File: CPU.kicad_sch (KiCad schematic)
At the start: 12 parts, among them U3 MOS6502

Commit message: update traces
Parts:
- B11, C11, C14: footprint Apple:DIP-14_W7.62mm -> Package_DIP:DIP-14_W7.62mm
- B6, B7, H10, H11, H3, H4, H5: footprint Apple:DIP-16_W7.62mm -> Package_DIP:DIP-16_W7.62mm
- H7: renamed from U3; footprint Apple:DIP-40_W15.24mm -> Package_DIP:DIP-40_W15.24mm
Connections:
- net ~{RDY} renamed RDY
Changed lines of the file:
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@@
   (junction (at 177.292 107.95) (diameter 0) (color 0 0 0 0)
   )
+  (junction (at 213.36 114.3) (diameter 0) (color 0 0 0 0)
+  )
   (junction (at 134.112 94.234) (diameter 0) (color 0 0 0 0)
   )
@@
   (junction (at 270.256 110.49) (diameter 0) (color 0 0 0 0)
   )
+  (junction (at 222.25 129.54) (diameter 0) (color 0 0 0 0)
+  )
   (junction (at 270.51 82.55) (diameter 0) (color 0 0 0 0)
   )
@@
   (junction (at 270.256 137.668) (diameter 0) (color 0 0 0 0)
   )
+  (junction (at 215.9 123.444) (diameter 0) (color 0 0 0 0)
+  )
   (bus_entry (at 138.43 252.73) (size 2.54 2.54)
     (stroke (width 0) (type default))
@@
     (stroke (width 0) (type default))
   )
+  (wire (pts (xy 215.9 123.444) (xy 215.9 116.84))
+    (stroke (width 0) (type default))
+  )
   (wire (pts (xy 165.608 126.238) (xy 156.972 126.238))
     (stroke (width 0) (type default))
@@
     (stroke (width 0) (type default))
   )
+  (wire (pts (xy 215.392 123.444) (xy 215.9 123.444))
+    (stroke (width 0) (type default))
+  )
   (wire (pts (xy 268.224 159.004) (xy 271.78 159.004))
     (stroke (width 0) (type default))
@@
     (stroke (width 0) (type default))
   )
-  (wire (pts (xy 215.9 127) (xy 215.9 116.84))
+  (wire (pts (xy 215.9 127) (xy 215.9 123.444))
     (stroke (width 0) (type default))
   )
@@
     (stroke (width 0) (type default))
   )
+  (wire (pts (xy 222.25 129.54) (xy 222.25 130.302))
+    (stroke (width 0) (type default))
+  )
   (wire (pts (xy 165.608 121.158) (xy 156.972 121.158))
     (stroke (width 0) (type default))
@@
     (stroke (width 0) (type default))
   )
-  (wire (pts (xy 222.25 129.54) (xy 222.25 121.92))
+  (wire (pts (xy 222.25 121.92) (xy 222.25 129.54))
     (stroke (width 0) (type default))
   )
@@
   )
   (wire (pts (xy 248.92 97.79) (xy 256.032 97.79))
+    (stroke (width 0) (type default))
+  )
+  (wire (pts (xy 213.106 114.3) (xy 213.36 114.3))
     (stroke (width 0) (type default))
   )
@@
     (effects (font (size 1.27 1.27)) (justify left))
     (property "Intersheetrefs" "${INTERSHEET_REFS}" (at 200.66 124.46 0)
+      (effects (font (size 1.27 1.27)) hide)
+    )
+  )
+  (global_label "~{IRQ}" (shape output) (at 215.392 123.444 180)
+    (effects (font (size 0.9906 0.9906)) (justify right))
+    (property "Intersheetrefs" "${INTERSHEET_REFS}" (at 215.392 123.444 0)
       (effects (font (size 1.27 1.27)) hide)
     )
@@
     )
   )
+  (global_label "RDY" (shape output) (at 222.25 130.302 270)
+    (effects (font (size 0.9906 0.9906)) (justify right))
+    (property "Intersheetrefs" "${INTERSHEET_REFS}" (at 222.25 130.302 0)
+      (effects (font (size 1.27 1.27)) hide)
+    )
+  )
   (global_label "~{KBD}" (shape input) (at 44.704 260.35 180)
     (effects (font (size 1.27 1.27)) (justify right))
@@
     (effects (font (size 1.27 1.27)) (justify left))
     (property "Intersheetrefs" "${INTERSHEET_REFS}" (at 304.546 83.566 0)
+      (effects (font (size 1.27 1.27)) hide)
+    )
+  )
+  (global_label "~{NMI}" (shape output) (at 213.106 114.3 180)
+    (effects (font (size 0.9906 0.9906)) (justify right))
+    (property "Intersheetrefs" "${INTERSHEET_REFS}" (at 213.106 114.3 0)
       (effects (font (size 1.27 1.27)) hide)
     )
@@
       (effects (font (size 1.27 1.27)))
     )
-    (property "Footprint" "Apple:DIP-14_W7.62mm" (at 201.422 98.044 0)
+    (property "Footprint" "Package_DIP:DIP-14_W7.62mm" (at 201.422 98.044 0)
       (effects (font (size 1.27 1.27)) hide)
     )
@@
       (effects (font (size 1.27 1.27)))
     )
-    (property "Footprint" "Apple:DIP-14_W7.62mm" (at 189.484 107.95 0)
+    (property "Footprint" "Package_DIP:DIP-14_W7.62mm" (at 189.484 107.95 0)
       (effects (font (size 1.27 1.27)) hide)
     )
@@
       (effects (font (size 1.27 1.27)))
     )
-    (property "Footprint" "Apple:DIP-16_W7.62mm" (at 282.194 89.662 0)
+    (property "Footprint" "Package_DIP:DIP-16_W7.62mm" (at 282.194 89.662 0)
       (effects (font (size 1.27 1.27)) hide)
     )
@@
       (effects (font (size 1.27 1.27)))
     )
-    (property "Footprint" "Apple:DIP-16_W7.62mm" (at 146.812 86.614 0)
+    (property "Footprint" "Package_DIP:DIP-16_W7.62mm" (at 146.812 86.614 0)
       (effects (font (size 1.27 1.27)) hide)
     )
@@
       (effects (font (size 1.27 1.27)))
     )
-    (property "Footprint" "Apple:DIP-16_W7.62mm" (at 146.812 127.254 0)
+    (property "Footprint" "Package_DIP:DIP-16_W7.62mm" (at 146.812 127.254 0)
       (effects (font (size 1.27 1.27)) hide)
     )
@@
       (effects (font (size 1.27 1.27)))
     )
-    (property "Footprint" "Apple:DIP-16_W7.62mm" (at 282.194 117.602 0)
+    (property "Footprint" "Package_DIP:DIP-16_W7.62mm" (at 282.194 117.602 0)
       (effects (font (size 1.27 1.27)) hide)
     )
@@
       (effects (font (size 1.27 1.27)))
     )
-    (property "Footprint" "Apple:DIP-16_W7.62mm" (at 282.702 144.78 0)
+    (property "Footprint" "Package_DIP:DIP-16_W7.62mm" (at 282.702 144.78 0)
       (effects (font (size 1.27 1.27)) hide)
     )
@@
       (effects (font (size 1.27 1.27)))
     )
-    (property "Footprint" "Apple:DIP-14_W7.62mm" (at 260.35 63.5 0)
+    (property "Footprint" "Package_DIP:DIP-14_W7.62mm" (at 260.35 63.5 0)
       (effects (font (size 1.27 1.27)) hide)
     )
@@
       (effects (font (size 1.27 1.27)))
     )
-    (property "Footprint" "Apple:DIP-16_W7.62mm" (at 67.31 245.11 0)
+    (property "Footprint" "Package_DIP:DIP-16_W7.62mm" (at 67.31 245.11 0)
       (effects (font (size 1.27 1.27)) hide)
     )
@@
   (symbol (lib_id "AppleII-rescue:MOS6502-AppleII") (at 236.22 110.49 0) (unit 1)
     (in_bom yes) (on_board yes) (dnp no)
-    (property "Reference" "U3" (at 245.11 74.676 0)
+    (property "Reference" "H7" (at 245.11 74.676 0)
       (effects (font (size 1.27 1.27)))
     )
@@
       (effects (font (size 1.27 1.27)))
     )
-    (property "Footprint" "Apple:DIP-40_W15.24mm" (at 236.22 148.59 0)
+    (property "Footprint" "Package_DIP:DIP-40_W15.24mm" (at 236.22 148.59 0)
       (effects (font (size 1.27 1.27)) hide)
     )
@@
       (project "AppleII"
         (path "/f1f08369-4db3-46f7-9b89-a5d3cfbed55a/00000000-0000-0000-0000-00005fe9ff4d"
-          (reference "U3") (unit 1)
+          (reference "H7") (unit 1)
         )
       )
@@
       (effects (font (size 1.27 1.27)))
     )
-    (property "Footprint" "Apple:DIP-16_W7.62mm" (at 179.07 245.11 0)
-      (effects (font (size 1.27 1.27)) hide)
-    )
+    (property "Footprint" "Package_DIP:DIP-16_W7.62mm" (at 179.07 245.11 0)
+      (effects (font (size 1.27 1.27)) hide)
+    )

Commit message: more tracing
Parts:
- H7: value MOS6502 -> 6502
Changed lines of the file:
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@@
       (effects (font (size 1.27 1.27)))
     )
-    (property "Value" "MOS6502" (at 242.062 76.454 0)
+    (property "Value" "6502" (at 242.062 76.454 0)
       (effects (font (size 1.27 1.27)))
     )

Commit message: finish tracing
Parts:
- added Cap44: 0.1uF, Capacitor_THT:C_Disc_D5.0mm_W2.5mm_P5.00mm, symbol Device:C_Small
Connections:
- net +5V: now also Cap44.2
- net GND: now also Cap44.1
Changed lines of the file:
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@@
   (junction (at 270.256 123.19) (diameter 0) (color 0 0 0 0)
   )
+  (junction (at 67.31 222.25) (diameter 0) (color 0 0 0 0)
+  )
   (junction (at 270.256 110.49) (diameter 0) (color 0 0 0 0)
   )
@@
   (junction (at 36.83 203.2) (diameter 0) (color 0 0 0 0)
   )
+  (junction (at 41.91 186.69) (diameter 0) (color 0 0 0 0)
+  )
   (junction (at 157.734 114.554) (diameter 0) (color 0 0 0 0)
   )
@@
     (stroke (width 0) (type default))
   )
+  (bus_entry (at 41.91 227.33) (size 2.54 2.54)
+    (stroke (width 0) (type default))
+  )
   (bus_entry (at 256.032 95.25) (size 2.54 -2.54)
     (stroke (width 0) (type default))
   )
+  (bus_entry (at 153.67 242.57) (size 2.54 2.54)
+    (stroke (width 0) (type default))
+  )
   (bus_entry (at 128.27 81.534) (size 2.54 2.54)
     (stroke (width 0) (type default))
@@
     (stroke (width 0) (type default))
   )
+  (bus_entry (at 153.67 234.95) (size 2.54 2.54)
+    (stroke (width 0) (type default))
+  )
   (bus_entry (at 302.26 97.282) (size -2.54 2.54)
     (stroke (width 0) (type default))
@@
     (stroke (width 0) (type default))
   )
+  (bus_entry (at 153.67 250.19) (size 2.54 2.54)
+    (stroke (width 0) (type default))
+  )
   (bus_entry (at 36.83 252.73) (size 2.54 2.54)
     (stroke (width 0) (type default))
@@
     (stroke (width 0) (type default))
   )
+  (bus_entry (at 41.91 250.19) (size 2.54 2.54)
+    (stroke (width 0) (type default))
+  )
   (bus_entry (at 36.83 237.49) (size 2.54 2.54)
     (stroke (width 0) (type default))
@@
     (stroke (width 0) (type default))
   )
+  (bus_entry (at 153.67 227.33) (size 2.54 2.54)
+    (stroke (width 0) (type default))
+  )
   (bus_entry (at 256.032 110.49) (size 2.54 -2.54)
     (stroke (width 0) (type default))
@@
     (stroke (width 0) (type default))
   )
+  (bus_entry (at 41.91 242.57) (size 2.54 2.54)
+    (stroke (width 0) (type default))
+  )
   (bus_entry (at 256.032 87.63) (size 2.54 -2.54)
     (stroke (width 0) (type default))
@@
     (stroke (width 0) (type default))
   )
+  (bus (pts (xy 153.67 234.95) (xy 153.67 242.57))
+    (stroke (width 0) (type default))
+  )
   (wire (pts (xy 261.112 92.71) (xy 271.272 92.71))
     (stroke (width 0) (type default))
@@
     (stroke (width 0) (type default))
   )
+  (bus (pts (xy 41.91 242.57) (xy 41.91 250.19))
+    (stroke (width 0) (type default))
+  )
   (wire (pts (xy 213.36 114.3) (xy 213.36 121.92))
     (stroke (width 0) (type default))
@@
     (stroke (width 0) (type default))
   )
+  (wire (pts (xy 44.45 245.11) (xy 54.61 245.11))
+    (stroke (width 0) (type default))
+  )
   (wire (pts (xy 166.37 245.11) (xy 156.21 245.11))
     (stroke (width 0) (type default))
@@
     (stroke (width 0) (type default))
   )
+  (bus (pts (xy 41.91 227.33) (xy 41.91 242.57))
+    (stroke (width 0) (type default))
+  )
   (bus (pts (xy 258.572 142.748) (xy 258.572 145.288))
     (stroke (width 0) (type default))
@@
     (stroke (width 0) (type default))
   )
+  (bus (pts (xy 41.91 186.69) (xy 153.67 186.69))
+    (stroke (width 0) (type default))
+  )
   (wire (pts (xy 189.992 95.504) (xy 193.802 95.504))
     (stroke (width 0) (type default))
@@
     (stroke (width 0) (type default))
   )
-  (wire (pts (xy 44.196 229.87) (xy 54.61 229.87))
-    (stroke (width 0) (type default))
-  )
   (bus (pts (xy 258.572 85.09) (xy 258.572 87.63))
     (stroke (width 0) (type default))
@@
     (stroke (width 0) (type default))
   )
+  (bus (pts (xy 26.67 186.69) (xy 41.91 186.69))
+    (stroke (width 0) (type default))
+  )
   (wire (pts (xy 136.652 137.414) (xy 134.112 137.414))
     (stroke (width 0) (type default))
@@
     (stroke (width 0) (type default))
   )
+  (wire (pts (xy 44.45 252.73) (xy 54.61 252.73))
+    (stroke (width 0) (type default))
+  )
   (wire (pts (xy 130.81 89.154) (xy 134.112 89.154))
     (stroke (width 0) (type default))
@@
     (stroke (width 0) (type default))
   )
+  (bus (pts (xy 153.67 186.69) (xy 153.67 227.33))
+    (stroke (width 0) (type default))
+  )
   (wire (pts (xy 191.77 245.11) (xy 194.31 245.11))
     (stroke (width 0) (type default))
@@
     (stroke (width 0) (type default))
   )
+  (bus (pts (xy 153.67 227.33) (xy 153.67 234.95))
+    (stroke (width 0) (type default))
+  )
   (wire (pts (xy 134.112 96.774) (xy 134.112 94.234))
     (stroke (width 0) (type default))
@@
     (stroke (width 0) (type default))
   )
+  (wire (pts (xy 44.45 229.87) (xy 54.61 229.87))
+    (stroke (width 0) (type default))
+  )
   (bus (pts (xy 128.27 117.094) (xy 128.27 122.174))
     (stroke (width 0) (type default))
@@
     (stroke (width 0) (type default))
   )
+  (bus (pts (xy 153.67 242.57) (xy 153.67 250.19))
+    (stroke (width 0) (type default))
+  )
   (bus (pts (xy 85.09 210.82) (xy 85.09 227.33))
     (stroke (width 0) (type default))
@@
     (stroke (width 0) (type default))
   )
+  (bus (pts (xy 41.91 186.69) (xy 41.91 227.33))
+    (stroke (width 0) (type default))
+  )
   (wire (pts (xy 134.112 84.074) (xy 136.652 84.074))
     (stroke (width 0) (type default))
@@
     (stroke (width 0) (type default))
   )
-  (wire (pts (xy 44.196 252.73) (xy 54.61 252.73))
-    (stroke (width 0) (type default))
-  )
   (bus (pts (xy 138.43 203.2) (xy 138.43 229.87))
     (stroke (width 0) (type default))
@@
     (stroke (width 0) (type default))
   )
-  (wire (pts (xy 44.196 245.11) (xy 54.61 245.11))
-    (stroke (width 0) (type default))
-  )
   (bus (pts (xy 212.344 82.55) (xy 212.344 85.09))
     (stroke (width 0) (type default))
@@
   )
   (wire (pts (xy 261.112 145.288) (xy 271.78 145.288))
+    (stroke (width 0) (type default))
+  )
+  (wire (pts (xy 66.04 222.25) (xy 67.31 222.25))
     (stroke (width 0) (type default))
   )
@@
     (effects (font (size 1.27 1.27)) (justify left bottom))
   )
-  (label "KBD_Data6" (at 44.196 229.87 0) (fields_autoplaced)
+  (label "KBD_Data6" (at 44.45 229.87 0) (fields_autoplaced)
     (effects (font (size 1.27 1.27)) (justify left bottom))
   )
@@
     (effects (font (size 1.27 1.27)) (justify left bottom))
   )
-  (label "KBD_Data4" (at 44.196 252.73 0) (fields_autoplaced)
+  (label "KBD_Data4" (at 44.45 252.73 0) (fields_autoplaced)
     (effects (font (size 1.27 1.27)) (justify left bottom))
   )
@@
     (effects (font (size 1.27 1.27)) (justify left bottom))
   )
-  (label "KBD_Data5" (at 44.196 245.11 0) (fields_autoplaced)
+  (label "KBD_Data5" (at 44.45 245.11 0) (fields_autoplaced)
     (effects (font (size 1.27 1.27)) (justify left bottom))
   )
@@
   )
   (hierarchical_label "D[0..7]" (shape bidirectional) (at 27.94 72.39 180) (fields_autoplaced)
+    (effects (font (size 1.27 1.27)) (justify right))
+  )
+  (hierarchical_label "KBD_Data[0..6]" (shape input) (at 26.67 186.69 180) (fields_autoplaced)
     (effects (font (size 1.27 1.27)) (justify right))
   )
@@
         )
       )
+    )
+  )
+  (symbol (lib_id "power:GND") (at 60.96 222.25 270) (unit 1)
+    (in_bom yes) (on_board yes) (dnp no)
+    (property "Reference" "#PWR048" (at 54.61 222.25 0)
+      (effects (font (size 1.27 1.27)) hide)
+    )
+    (property "Value" "GND" (at 56.5658 222.377 0)
+      (effects (font (size 1.27 1.27)))
+    )
+    (property "Footprint" "" (at 60.96 222.25 0)
+      (effects (font (size 1.27 1.27)) hide)
+    )
+    (property "Datasheet" "" (at 60.96 222.25 0)
+      (effects (font (size 1.27 1.27)) hide)
+    )
+    (pin "1")
+    (instances
+      (project "AppleII"
+        (path "/f1f08369-4db3-46f7-9b89-a5d3cfbed55a/00000000-0000-0000-0000-000060210f9e"
+          (reference "#PWR048") (unit 1)
+        )
+        (path "/f1f08369-4db3-46f7-9b89-a5d3cfbed55a/00000000-0000-0000-0000-00005fe9ff4d"
+          (reference "#PWR049") (unit 1)
+        )
+      )
+    )
+  )
+  (symbol (lib_id "Device:C_Small") (at 63.5 222.25 90) (unit 1)
+    (in_bom yes) (on_board yes) (dnp no)
+    (property "Reference" "Cap44" (at 61.722 221.996 0)
+      (effects (font (size 1.27 1.27)) (justify left))
+    )
+    (property "Value" "0.1uF" (at 63.5 220.472 0)
+      (effects (font (size 1.27 1.27)) (justify left))
+    )
+    (property "Footprint" "Capacitor_THT:C_Disc_D5.0mm_W2.5mm_P5.00mm" (at 63.5 222.25 0)
+      (effects (font (size 1.27 1.27)) hide)
+    )
+    (property "Datasheet" "~" (at 63.5 222.25 0)
+      (effects (font (size 1.27 1.27)) hide)
+    )
+    (pin "1")
+    (pin "2")
+    (instances
+      (project "AppleII"
+        (path "/f1f08369-4db3-46f7-9b89-a5d3cfbed55a/00000000-0000-0000-0000-000060210f9e"
+          (reference "Cap44") (unit 1)
+        )
+        (path "/f1f08369-4db3-46f7-9b89-a5d3cfbed55a/00000000-0000-0000-0000-00005fe9ff4d"
+          (reference "Cap45") (unit 1)
+        )
+      )

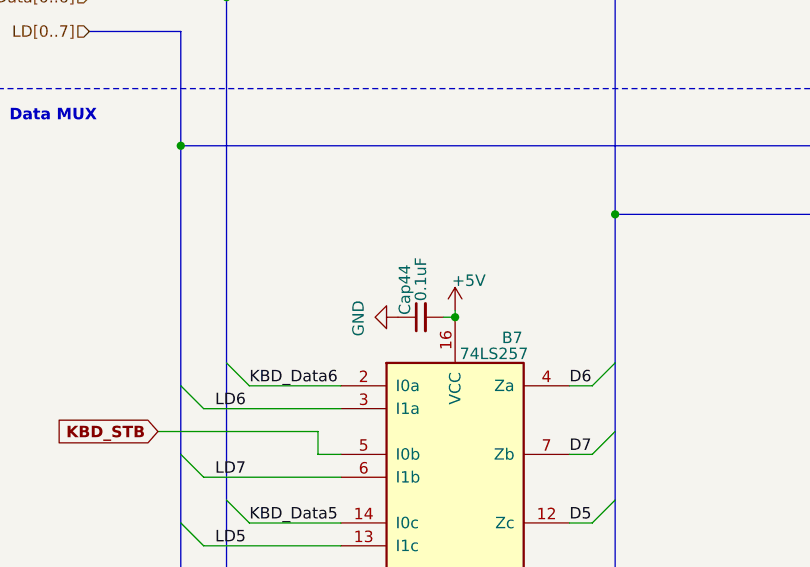
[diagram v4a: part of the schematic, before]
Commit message: beautify capacitor footprint
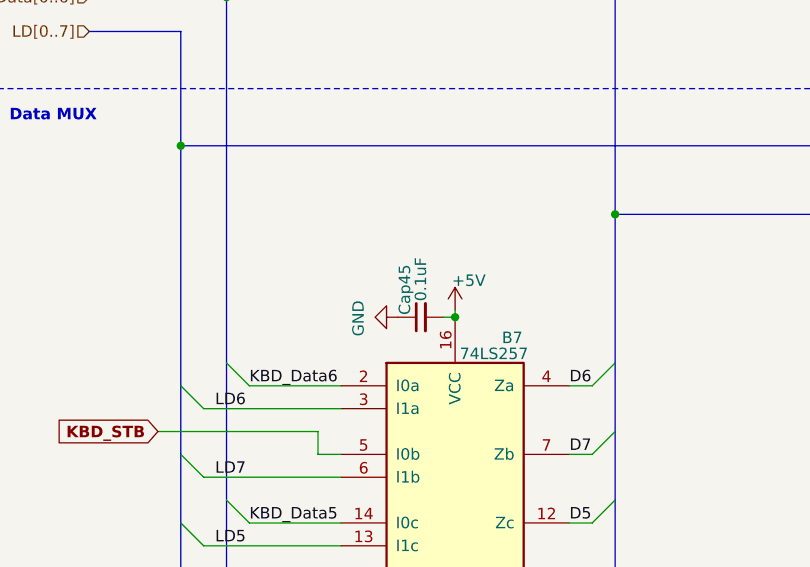
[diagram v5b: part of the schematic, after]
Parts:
- renumbered Cap44 to Cap45
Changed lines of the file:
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@@
   (symbol (lib_id "power:GND") (at 60.96 222.25 270) (unit 1)
     (in_bom yes) (on_board yes) (dnp no)
-    (property "Reference" "#PWR048" (at 54.61 222.25 0)
+    (property "Reference" "#PWR049" (at 54.61 222.25 0)
       (effects (font (size 1.27 1.27)) hide)
     )
@@
     (instances
       (project "AppleII"
-        (path "/f1f08369-4db3-46f7-9b89-a5d3cfbed55a/00000000-0000-0000-0000-000060210f9e"
-          (reference "#PWR048") (unit 1)
-        )
         (path "/f1f08369-4db3-46f7-9b89-a5d3cfbed55a/00000000-0000-0000-0000-00005fe9ff4d"
           (reference "#PWR049") (unit 1)
@@
   (symbol (lib_id "Device:C_Small") (at 63.5 222.25 90) (unit 1)
     (in_bom yes) (on_board yes) (dnp no)
-    (property "Reference" "Cap44" (at 61.722 221.996 0)
+    (property "Reference" "Cap45" (at 61.722 221.996 0)
       (effects (font (size 1.27 1.27)) (justify left))
     )
@@
     (instances
       (project "AppleII"
-        (path "/f1f08369-4db3-46f7-9b89-a5d3cfbed55a/00000000-0000-0000-0000-000060210f9e"
-          (reference "Cap44") (unit 1)
-        )
         (path "/f1f08369-4db3-46f7-9b89-a5d3cfbed55a/00000000-0000-0000-0000-00005fe9ff4d"
           (reference "Cap45") (unit 1)

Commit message: beautify resistors
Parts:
- Cap45: footprint Capacitor_THT:C_Disc_D5.0mm_W2.5mm_P5.00mm -> Apple-II:C_Disc_D5.0mm_W2.5mm_P5.00mm
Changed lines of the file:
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@@
       (effects (font (size 1.27 1.27)) (justify left))
     )
-    (property "Footprint" "Capacitor_THT:C_Disc_D5.0mm_W2.5mm_P5.00mm" (at 63.5 222.25 0)
+    (property "Footprint" "Apple-II:C_Disc_D5.0mm_W2.5mm_P5.00mm" (at 63.5 222.25 0)
       (effects (font (size 1.27 1.27)) hide)
     )
